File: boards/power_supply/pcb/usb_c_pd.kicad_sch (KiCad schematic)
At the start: 37 parts, among them J201 Conn_01x04_Socket, J202 12401826E412A, J203 USB IDC, SW201 SW_SPST, U201 USBLC6-2SC6

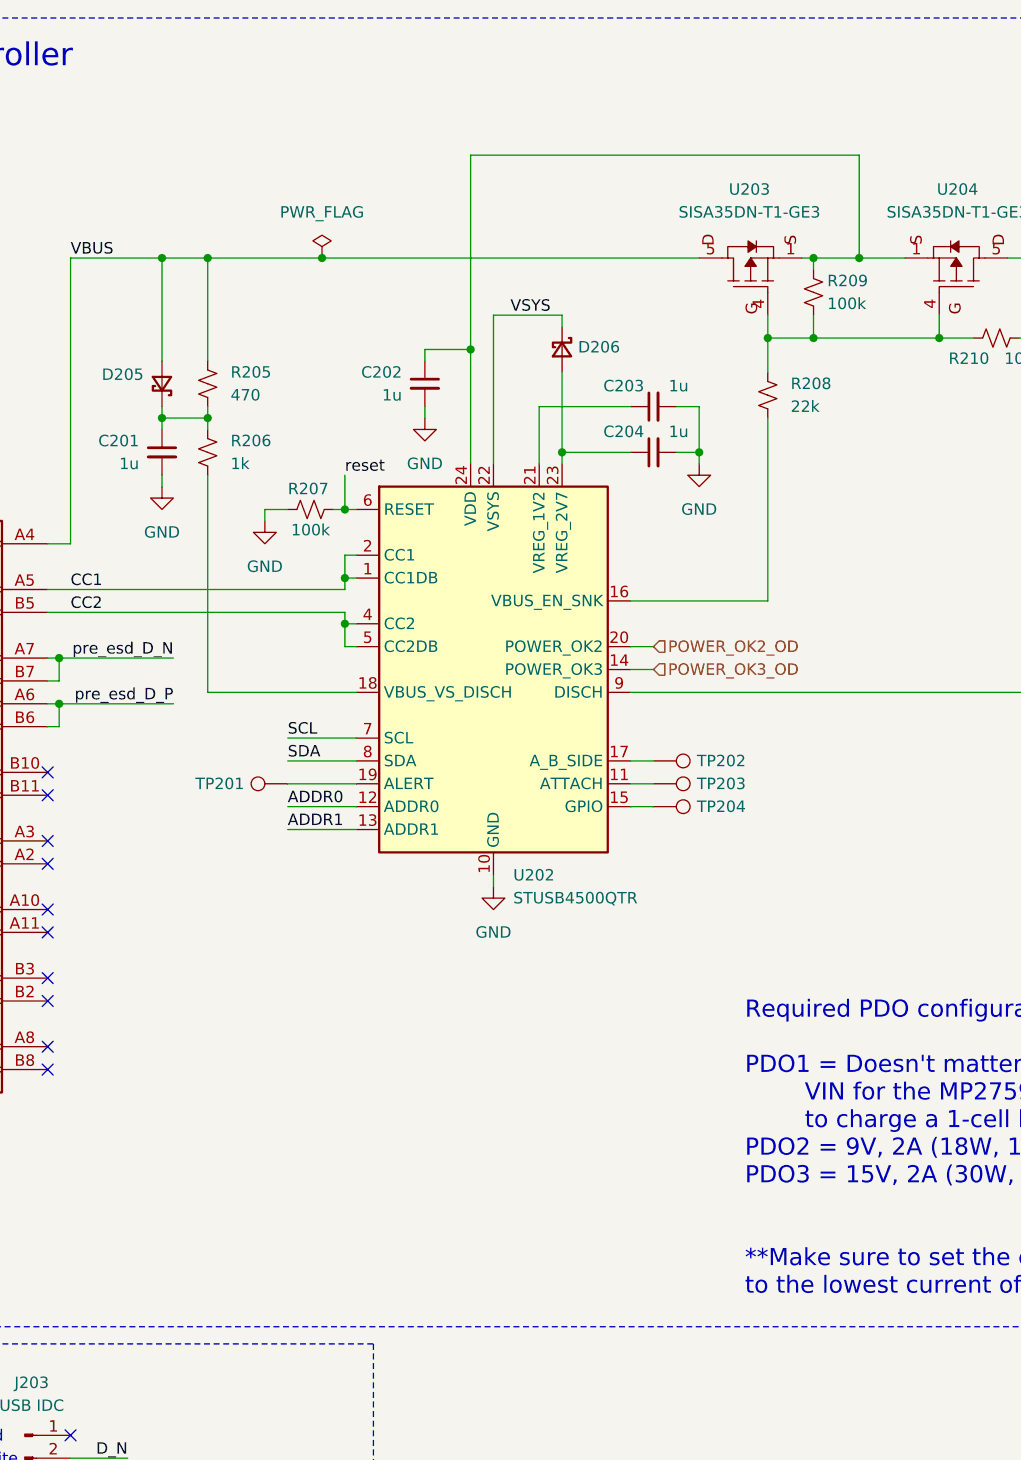
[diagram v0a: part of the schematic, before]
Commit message: psu schematic capture
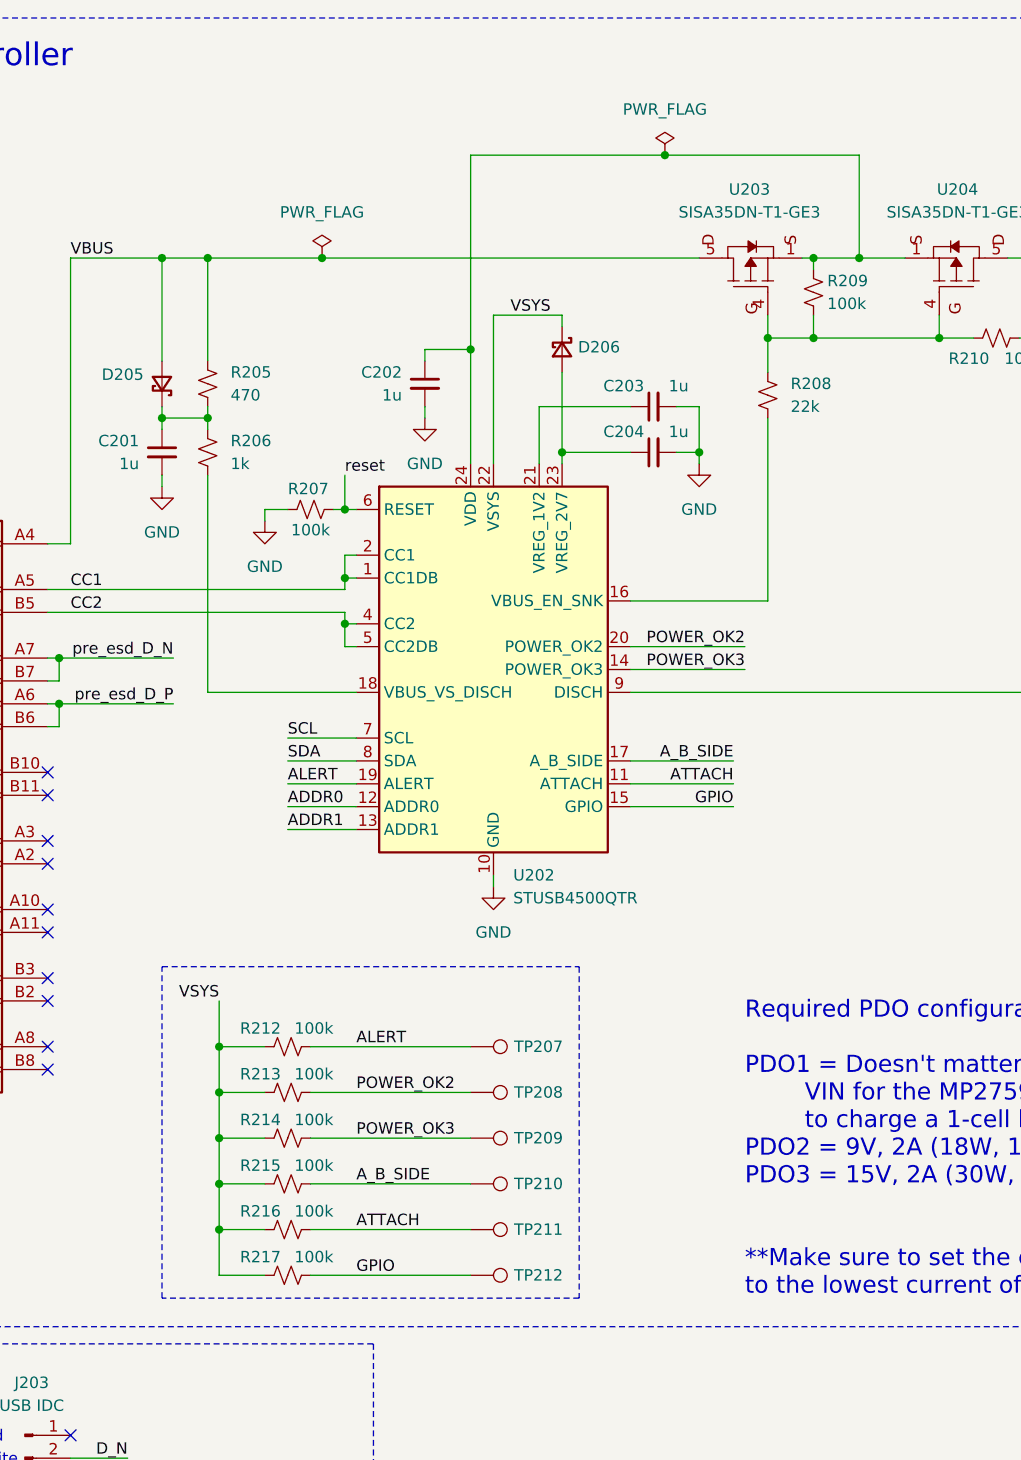
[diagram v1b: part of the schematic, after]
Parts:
- removed TP201, TP202, TP203, TP204: TestPoint, symbol Connector:TestPoint
- added R212, R213, R214, R215, R216, R217: 100k, symbol Device:R_Small_US
- added TP207, TP208, TP209, TP210, TP211, TP212: TestPoint, symbol Connector:TestPoint
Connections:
- net VSYS: now also R212.1, R213.1, R214.1, R215.1, R216.1, R217.1
- net GPIO: now reaches U202.15 (GPIO)
- net GPIO: now also R217.2, TP212.1
- net ATTACH: now reaches U202.11 (ATTACH)
- net ATTACH: now also R216.2, TP211.1
- net A_B_SIDE: now reaches U202.17 (A_B_SIDE)
- net A_B_SIDE: now also R215.2, TP210.1
- net ALERT: now reaches U202.19 (ALERT)
- net ALERT: now also R212.2, TP207.1
- net POWER_OK2_OD renamed POWER_OK2
- net POWER_OK2: now also R213.2, TP208.1
- net POWER_OK3_OD renamed POWER_OK3
- net POWER_OK3: now also R214.2, TP209.1

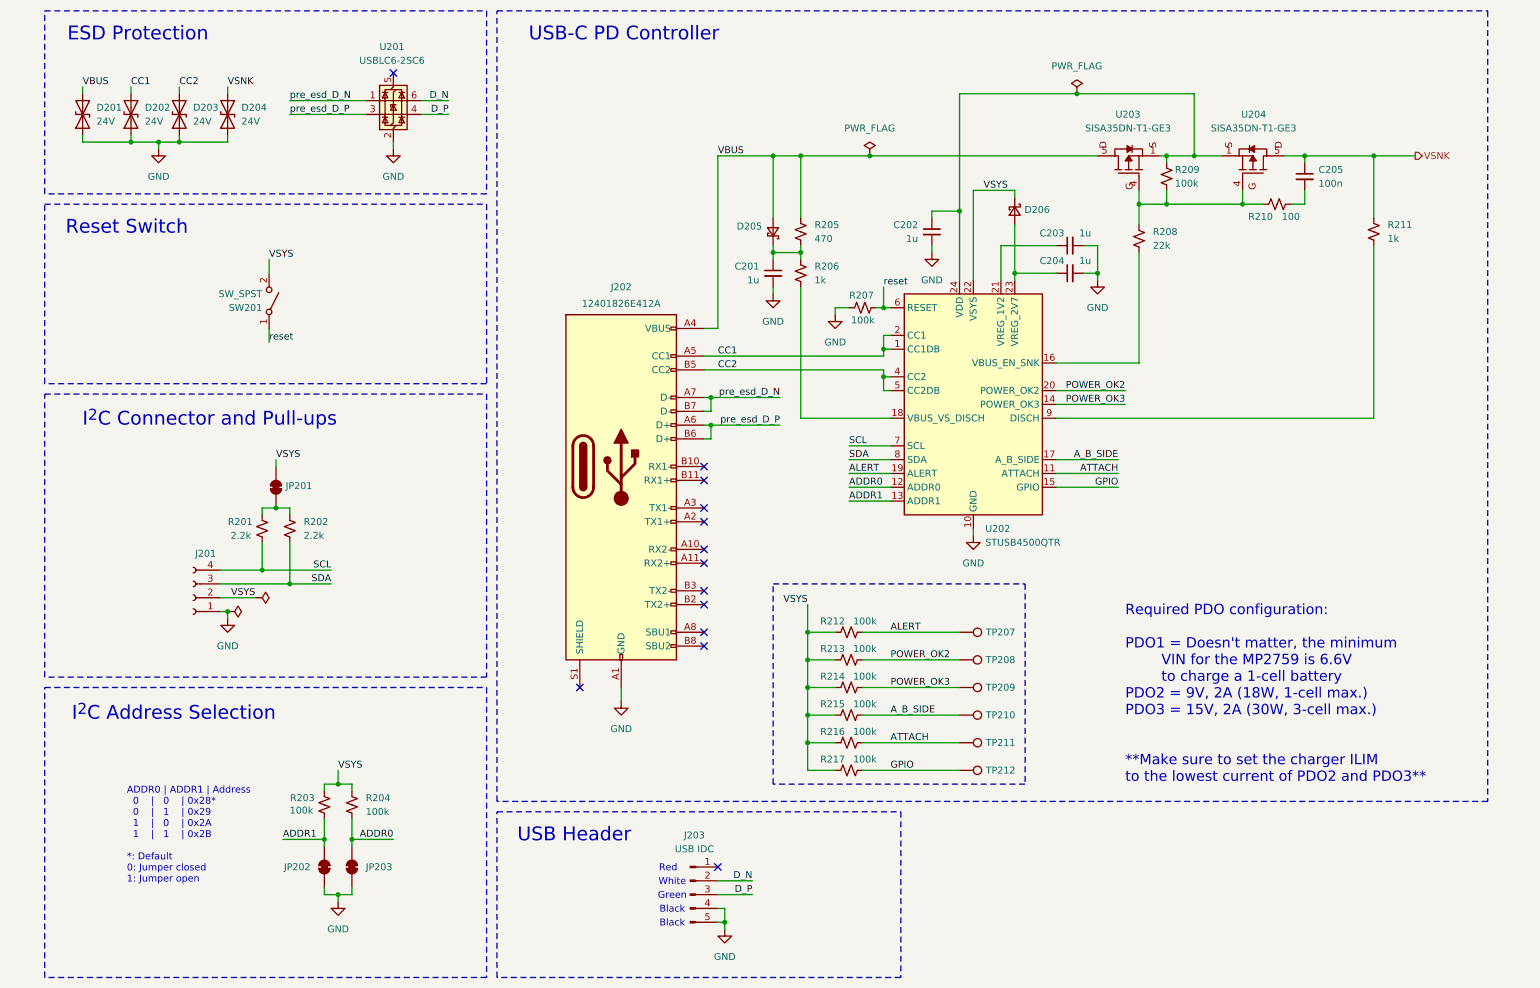
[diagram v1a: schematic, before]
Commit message: psu component selection
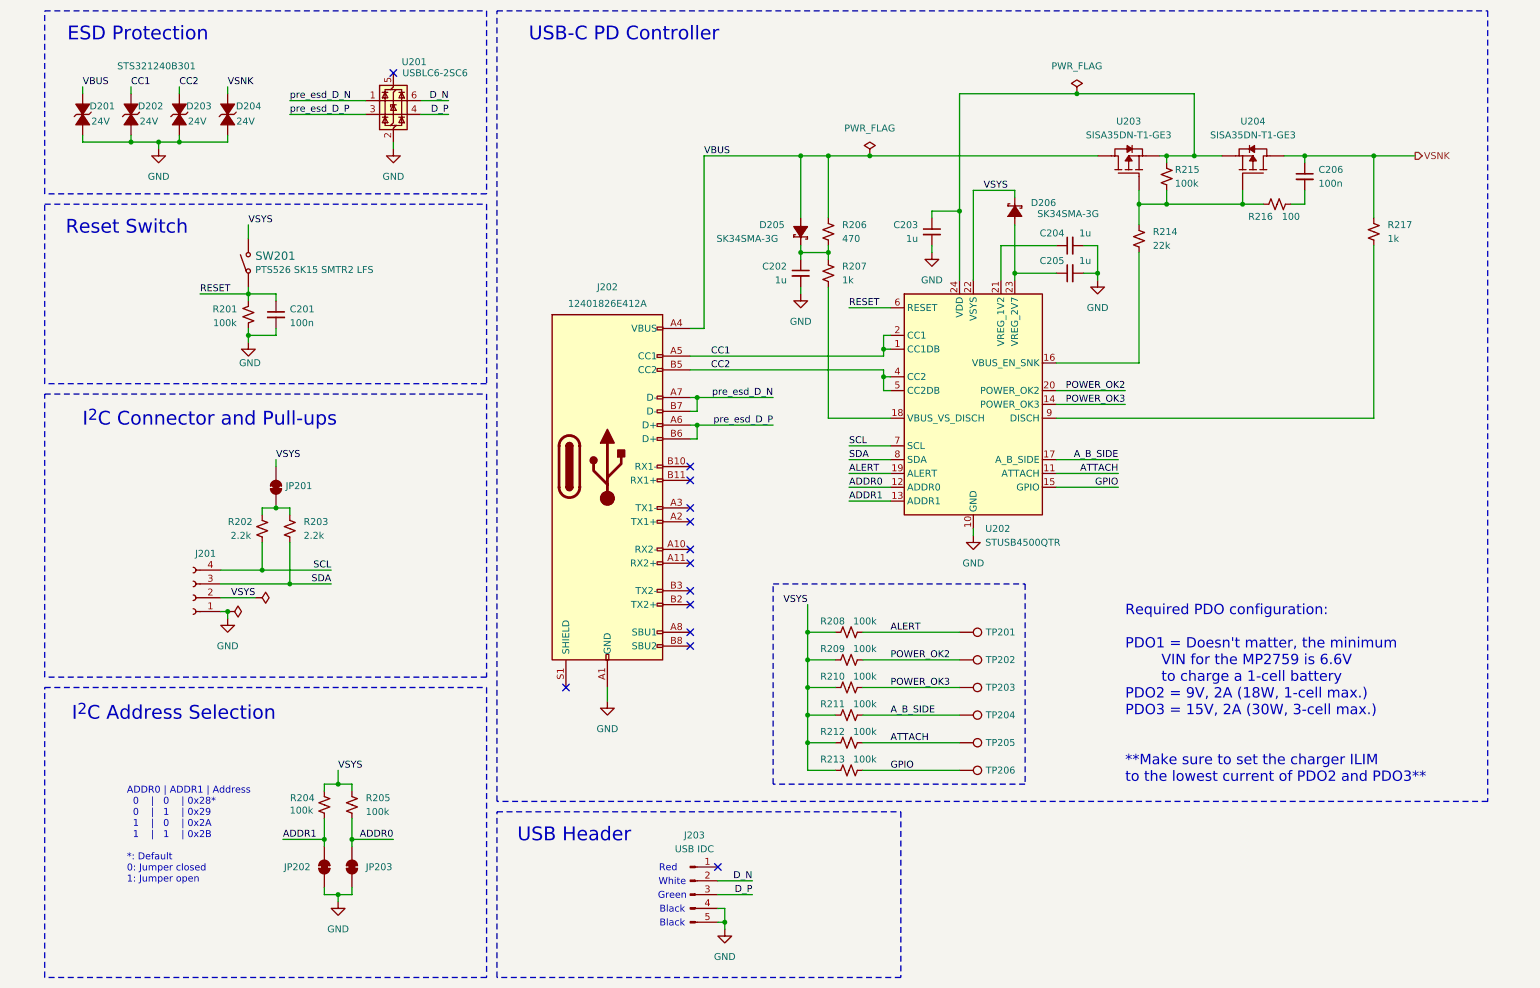
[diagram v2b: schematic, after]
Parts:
- removed D201, D202, D203, D204: 24V, symbol Device:D_TVS
- removed D205, D206: D_Schottky_Small, symbol Device:D_Schottky_Small
- removed R207: 100k, symbol Device:R_Small_US
- removed SW201: SW_SPST, symbol Switch:SW_SPST
- added C201: 100n, symbol Device:C_Small
- added D201, D202, D203, D204: 24V, symbol STS321240B301:STS321240B301
- added D205, D206: ~, symbol SK34SMA-3G:SK34SMA-3G
- added R201: 100k, symbol Device:R_Small_US
- added SW201: PTS526 SK15 SMTR2 LFS, SMT_FS, symbol PTS526_SK15_SMTR2_LFS:PTS526_SK15_SMTR2_LFS
- U201: value USBLC6-2SC6 -> USBLC6-2P6; MPN (none) -> USBLC6-2SC6
- renumbered C201 to C202, C202 to C203, C203 to C204, C204 to C205, C205 to C206, R201 to R202, R202 to R203, R203 to R204, R204 to R205, R205 to R206, R206 to R207, R212 to R208, R213 to R209, R214 to R210, R215 to R211, R216 to R212, R217 to R213, R208 to R214, R209 to R215, R210 to R216, R211 to R217, TP207 to TP201, TP208 to TP202, TP209 to TP203, TP210 to TP204, TP211 to TP205, TP212 to TP206
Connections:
- net CC1: now also D202.2
- net CC2: now also D203.2
- net GND: now also C201.2, D201.1, D202.1, D203.1, D204.1, R201.1
- net VBUS: now also D201.2, D205.2
- net VSNK: now also D204.2
- net VSYS: now also D206.1, SW201.3, SW201.4
- net at C205.1, U202.23 (VREG_2V7): now also D206.2
- net at C202.1, R206.2, R207.1: now also D205.1
- net reset renamed RESET
- net RESET: now also C201.1, R201.2, SW201.1, SW201.2
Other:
- moved on the sheet: C202, J202, R206, R207

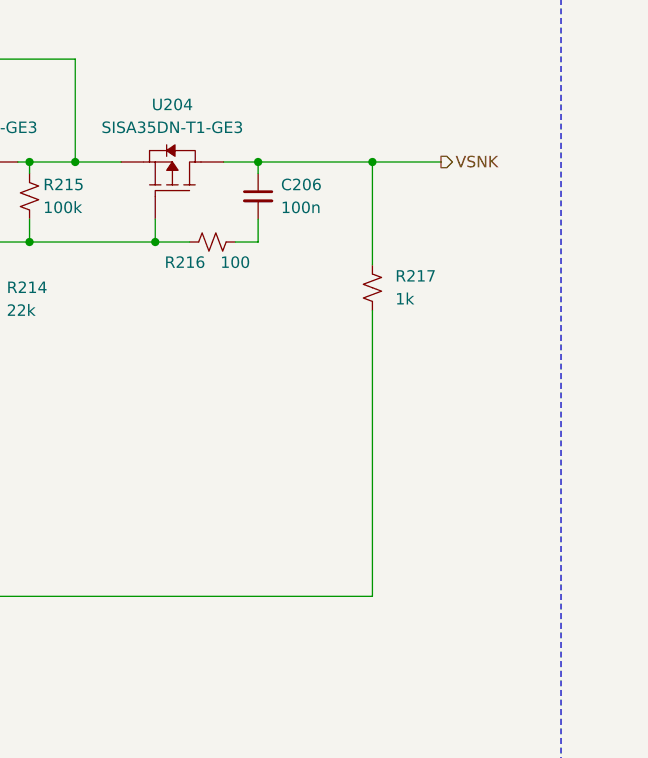
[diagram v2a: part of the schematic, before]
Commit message: created psu footprints
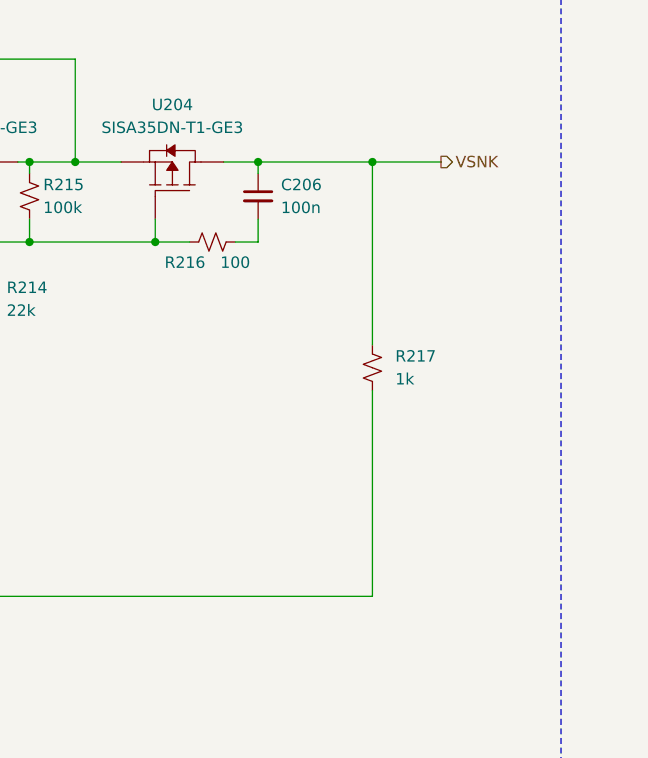
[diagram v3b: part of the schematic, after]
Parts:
- D201, D202, D203, D204: footprint (none) -> STS321240B301:STS321240B301
- D205, D206: footprint (none) -> SK34SMA-3G:SK34SMA-3G
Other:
- moved on the sheet: R217
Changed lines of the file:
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@@
 	(wire
 		(pts
-			(xy 260.35 91.44) (xy 260.35 59.69)
+			(xy 260.35 91.44) (xy 260.35 68.58)
 		)
 		(stroke
@@
 	(wire
 		(pts
-			(xy 260.35 43.18) (xy 260.35 54.61)
+			(xy 260.35 43.18) (xy 260.35 63.5)
 		)
 		(stroke
@@
 			)
 		)
-		(property "Footprint" ""
+		(property "Footprint" "STS321240B301:STS321240B301"
 			(at 20.32 35.56 0)
 			(effects
@@
 	(symbol
 		(lib_id "Device:R_Small_US")
-		(at 260.35 57.15 0)
+		(at 260.35 66.04 0)
 		(unit 1)
 		(exclude_from_sim no)
@@
 		(fields_autoplaced yes)
 		(property "Reference" "R217"
-			(at 262.89 55.8799 0)
+			(at 262.89 64.7699 0)
 			(effects
 				(font
@@
 		)
 		(property "Value" "1k"
-			(at 262.89 58.4199 0)
+			(at 262.89 67.3099 0)
 			(effects
 				(font
@@
 		)
 		(property "Footprint" ""
-			(at 260.35 57.15 0)
+			(at 260.35 66.04 0)
 			(effects
 				(font
@@
 		)
 		(property "Datasheet" "~"
-			(at 260.35 57.15 0)
+			(at 260.35 66.04 0)
 			(effects
 				(font
@@
 		)
 		(property "Description" "Resistor, small US symbol"
-			(at 260.35 57.15 0)
+			(at 260.35 66.04 0)
 			(effects
 				(font
@@
 			)
 		)
-		(property "Footprint" ""
+		(property "Footprint" "STS321240B301:STS321240B301"
 			(at 29.21 35.56 0)
 			(effects
@@
 			)
 		)
-		(property "Footprint" ""
+		(property "Footprint" "SK34SMA-3G:SK34SMA-3G"
 			(at 190.5 54.61 0)
 			(effects
@@
 			)
 		)
-		(property "Footprint" ""
+		(property "Footprint" "STS321240B301:STS321240B301"
 			(at 46.99 35.56 0)
 			(effects
@@
 			)
 		)
-		(property "Footprint" ""
+		(property "Footprint" "SK34SMA-3G:SK34SMA-3G"
 			(at 158.75 55.88 0)
 			(effects
@@
 			)
 		)
-		(property "Footprint" ""
+		(property "Footprint" "STS321240B301:STS321240B301"
 			(at 38.1 35.56 0)
 			(effects
